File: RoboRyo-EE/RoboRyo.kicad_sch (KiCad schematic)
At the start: 78 parts, among them IC2 LD29080DT33R, IC3 LD29080DT50R, J1 2601-1103_000-004, J2 2601-1103_000-004, J3 2601-1103_000-004, J4 2601-1103_000-004, J5 2601-1103_000-004, J6 2601-1103_000-004, J7 2601-1103_000-004, J8 2601-1103_000-004, Q1 DMG9926USD-13, Q2 DMG9926USD-13, Q3 DMG9926USD-13, Q4 DMG9926USD-13, Q5 DMG9926USD-13, Q6 DMG9926USD-13, Q7 CSD13383F4, U1 STM32F446RETx, U2 ATmega328P-MM, Y1 ABM3-16.000MHZ-D2Y-T

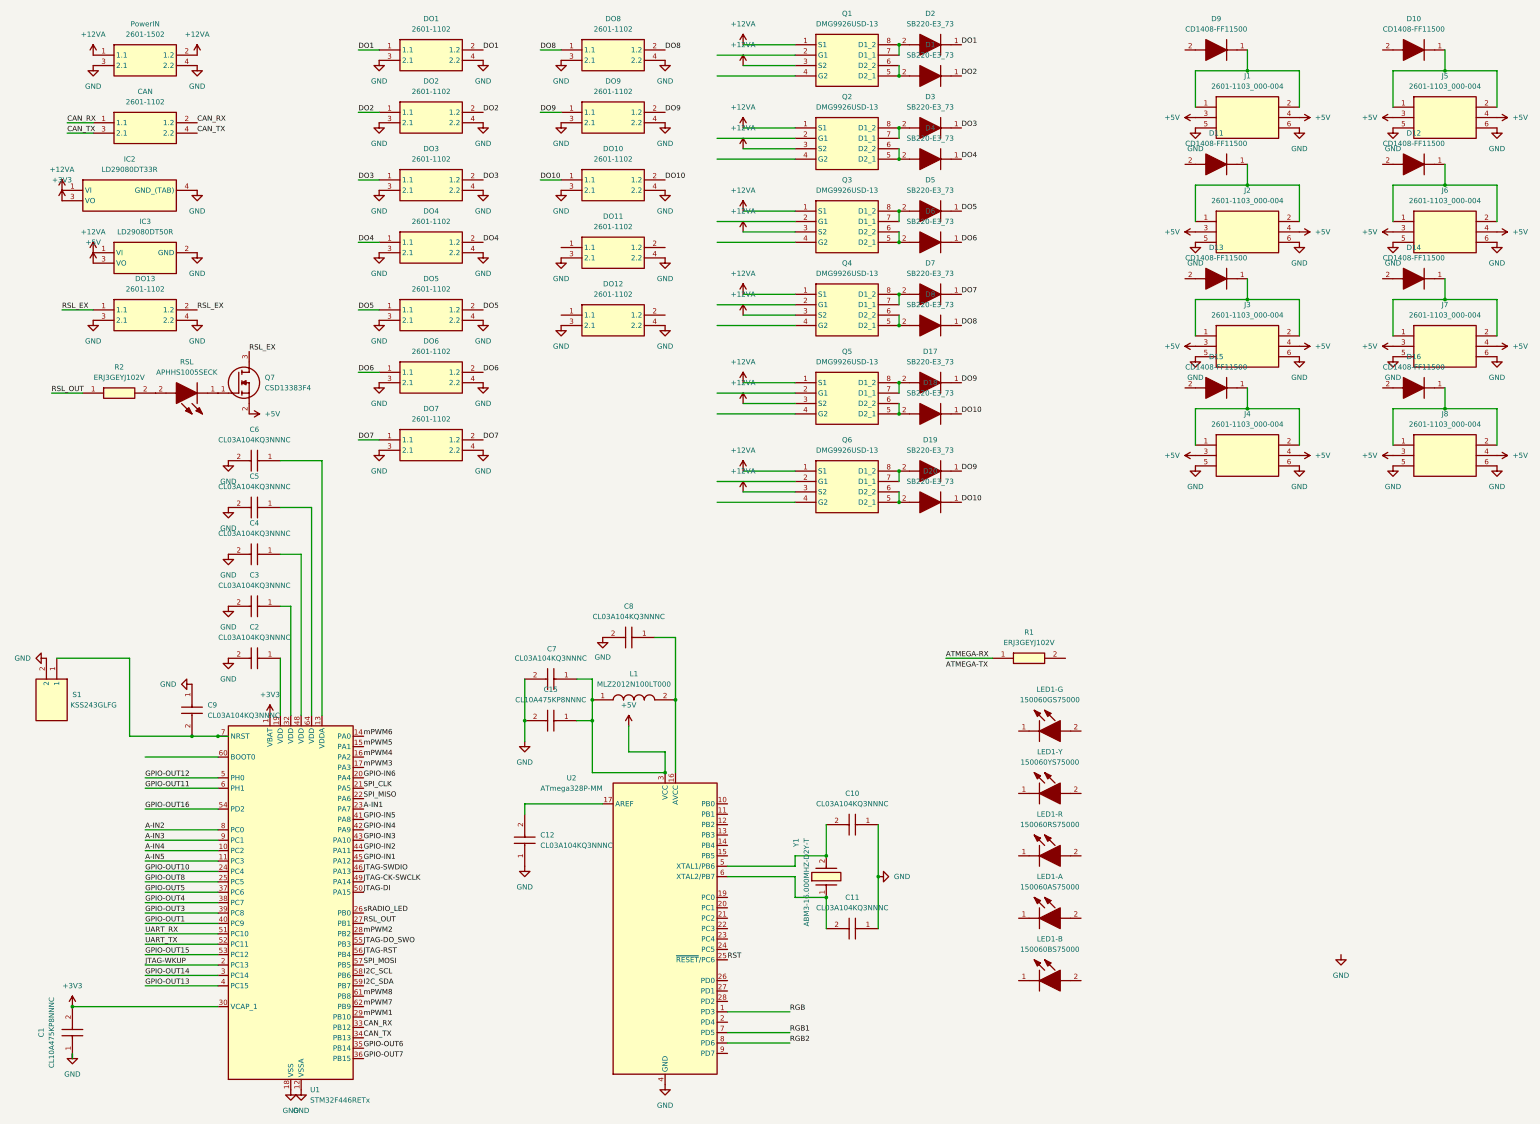
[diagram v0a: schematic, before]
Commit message: Sch New: IMU, Radio, PowerConfiguration
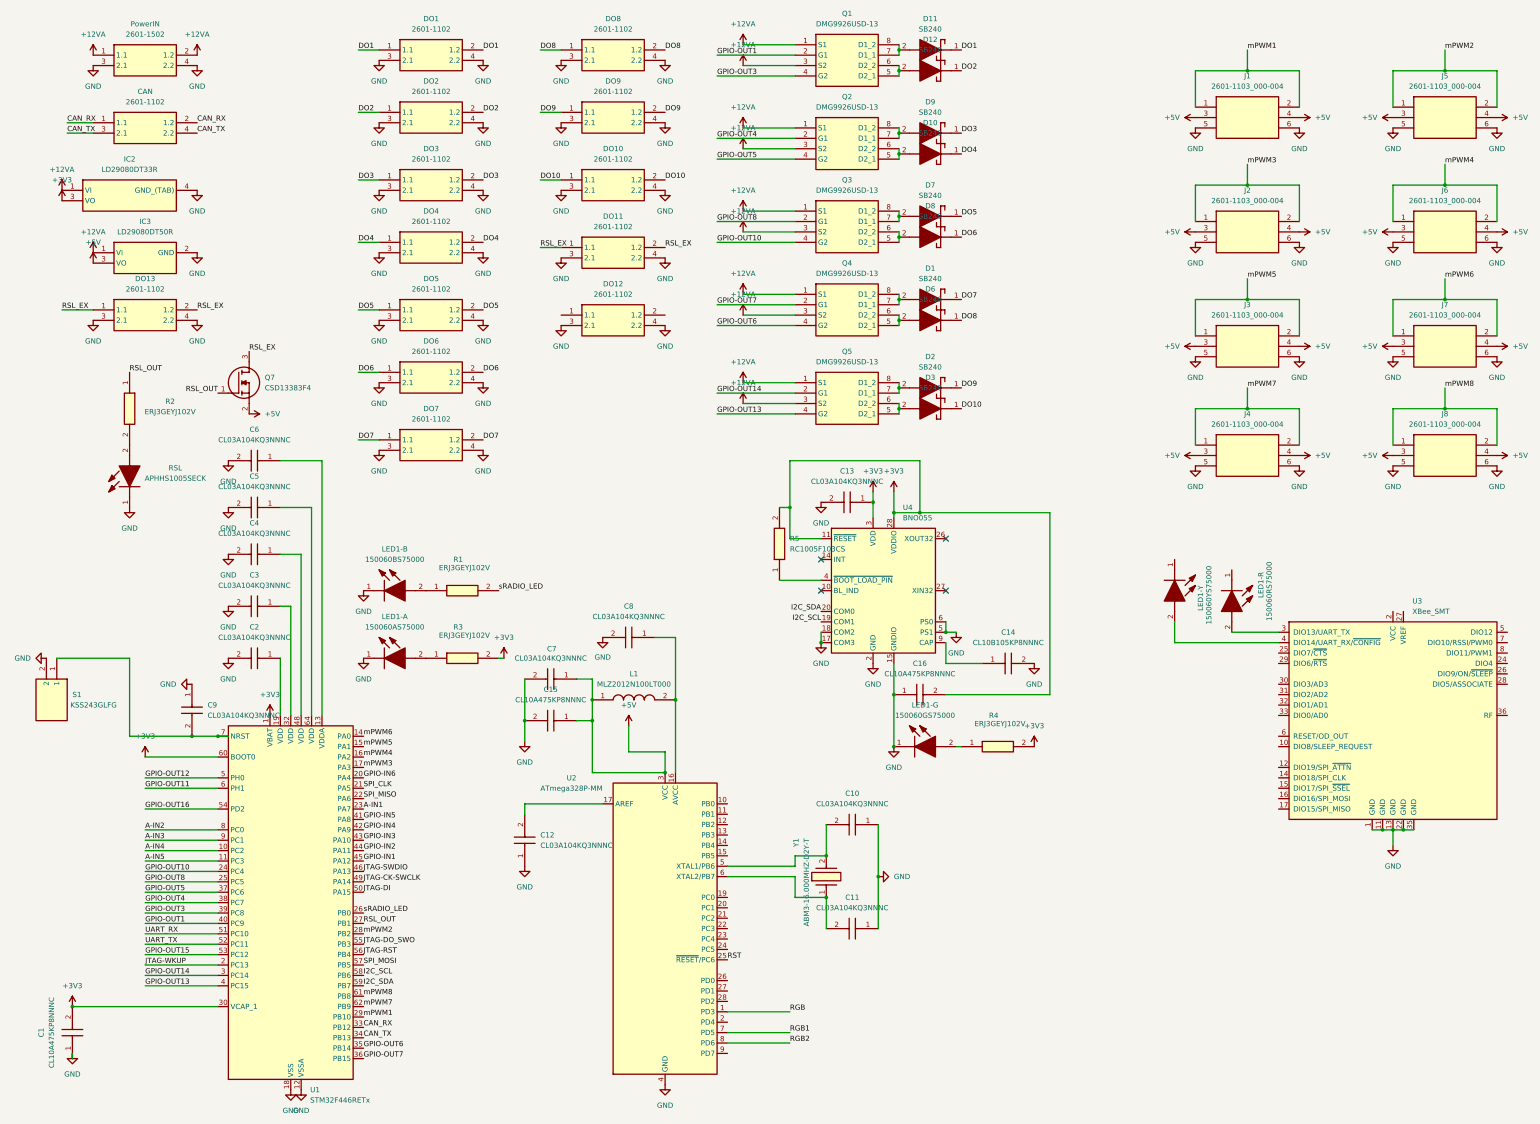
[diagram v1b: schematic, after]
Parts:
- removed D1, D17, D18, D19, D2, D20, D3, D4, D5, D6, D7, D8: SB220-E3_73, DIOAD1910W86L670D310, symbol SamacSys_Parts:SB220-E3_73
- removed D10, D11, D12, D13, D14, D15, D16, D9: CD1408-FF11500, DIOC3419X135N, symbol SamacSys_Parts:CD1408-FF11500
- removed Q6: DMG9926USD-13, SOIC127P600X175-8N, symbol SamacSys_Parts:DMG9926USD-13
- added C13: CL03A104KQ3NNNC, CAPC0603X33N, symbol SamacSys_Parts:CL03A104KQ3NNNC
- added C14: CL10B105KP8NNNC, CAPC1608X90N, symbol SamacSys_Parts:CL10B105KP8NNNC
- added C16: CL10A475KP8NNNC, CAPC1608X90N, symbol SamacSys_Parts:CL10A475KP8NNNC
- added D1, D10, D11, D12, D2, D3, D6, D7, D8, D9: SB240, DIOAD1910W86L670D310, symbol SamacSys_Parts:SB240
- added R3, R4: ERJ3GEYJ102V, ERJ3EKF1000V, symbol SamacSys_Parts:ERJ3GEYJ102V
- added R5: RC1005F103CS, RESC1005X40N, symbol SamacSys_Parts:RC1005F103CS
- added U3: XBee_SMT, RF_Module:Digi_XBee_SMT, symbol RF_ZigBee:XBee_SMT
- added U4: BNO055, Package_LGA:LGA-28_5.2x3.8mm_P0.5mm, symbol Sensor_Motion:BNO055
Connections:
- net ATMEGA-RX is gone; now on an unnamed net: R1.1
- net +3V3: now also U1.60 (BOOT0), C13.1, C16.2, R3.2, R4.2, R5.2, U4.11 (~{RESET}), U4.28 (VDDIO), U4.3 (VDD)
- net DO1: now also D11.1 (K)
- net DO10: now also D3.1 (K)
- net DO2: now also D12.1 (K)
- net DO3: now also D9.1 (K)
- net DO4: now also D10.1 (K)
- net DO5: now also D7.1 (K)
- net DO6: now also D8.1 (K)
- net DO7: now also D1.1 (K)
- net DO8: now also D6.1 (K)
- net DO9: now also D2.1 (K)
- net GND: now also LED1-A.1 (K), LED1-B.1 (K), LED1-G.1 (K), RSL.1 (K), C13.2, C14.2, C16.1, U3.1 (GND), U3.11 (GND), U3.13 (GND), U3.22 (GND), U3.35 (GND), U4.15 (GNDIO), U4.16 (GNDIO), U4.17 (COM3), U4.18 (COM2), U4.2 (GND), U4.25 (GNDIO), U4.5 (PS1), U4.6 (PS0)
- net GPIO-OUT1: now also Q1.2 (G1)
- net GPIO-OUT10: now also Q3.4 (G2)
- net GPIO-OUT13: now also Q5.4 (G2)
- net GPIO-OUT14: now also Q5.2 (G1)
- net GPIO-OUT3: now also Q1.4 (G2)
- net GPIO-OUT4: now also Q2.2 (G1)
- net GPIO-OUT5: now also Q2.4 (G2)
- net GPIO-OUT6: now also Q4.4 (G2)
- net GPIO-OUT7: now also Q4.2 (G1)
- net GPIO-OUT8: now also Q3.2 (G1)
- net I2C_SCL: now also U4.19 (COM1)
- net I2C_SDA: now also U4.20 (COM0)
- net RSL_EX: now also DO11.1 (1.1), DO11.2 (1.2)
- net RSL_OUT: now also Q7.1 (G)
- net mPWM1: now also J1.1 (1.1), J1.2 (1.2)
- net mPWM2: now also J5.1 (1.1), J5.2 (1.2)
- net mPWM3: now also J2.1 (1.1), J2.2 (1.2)
- net mPWM4: now also J6.1 (1.1), J6.2 (1.2)
- net mPWM5: now also J3.1 (1.1), J3.2 (1.2)
- net mPWM6: now also J7.1 (1.1), J7.2 (1.2)
- net mPWM7: now also J4.1 (1.1), J4.2 (1.2)
- net mPWM8: now also J8.1 (1.1), J8.2 (1.2)
- net sRADIO_LED: now also R1.2
- net at Q4.5 (D2_1), Q4.6 (D2_2): now also D6.2 (A)
- net at Q4.7 (D1_1), Q4.8 (D1_2): now also D1.2 (A)
- net at LED1-A.2 (A): now also R3.1
- net at Q1.7 (D1_1), Q1.8 (D1_2): now also D11.2 (A)
- net at Q1.5 (D2_1), Q1.6 (D2_2): now also D12.2 (A)
- net at Q3.5 (D2_1), Q3.6 (D2_2): now also D8.2 (A)
- net at Q2.7 (D1_1), Q2.8 (D1_2): now also D9.2 (A)
- net at LED1-R.2 (A): now also U3.3 (DIO13/UART_TX)
- net at Q3.7 (D1_1), Q3.8 (D1_2): now also D7.2 (A)
- net at LED1-Y.2 (A): now also U3.4 (DIO14/UART_RX/~{CONFIG})
- net at Q5.7 (D1_1), Q5.8 (D1_2): now also D2.2 (A)
- net at Q5.5 (D2_1), Q5.6 (D2_2): now also D3.2 (A)
- net at Q2.5 (D2_1), Q2.6 (D2_2): now also D10.2 (A)
- net at LED1-G.2 (A): now also R4.1
- new net: R5.1, U4.4 (~{BOOT_LOAD_PIN})
- new net: C14.1, U4.9 (CAP)
- no-connect marks 0 -> 4
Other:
- moved on the sheet: LED1-A, LED1-B, LED1-G, LED1-R, LED1-Y, R2, RSL

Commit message: Sch Complete, PCB: General Layout complete, wiring left
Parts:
- removed C10, C11, C12, C7, C8: CL03A104KQ3NNNC, CAPC0603X33N, symbol SamacSys_Parts:CL03A104KQ3NNNC
- removed C15: CL10A475KP8NNNC, CAPC1608X90N, symbol SamacSys_Parts:CL10A475KP8NNNC
- removed L1: MLZ2012N100LT000, INDC2012X105N, symbol SamacSys_Parts:MLZ2012N100LT000
- removed LED1-R: 150060RS75000, LEDC1608X80N, symbol SamacSys_Parts:150060RS75000
- removed LED1-Y: 150060YS75000, LEDC1608X80N, symbol SamacSys_Parts:150060YS75000
- removed U2: ATmega328P-MM, Package_DFN_QFN:QFN-28-1EP_4x4mm_P0.45mm_EP2.4x2.4mm, symbol MCU_Microchip_ATmega:ATmega328P-MM
- removed U3: XBee_SMT, RF_Module:Digi_XBee_SMT, symbol RF_ZigBee:XBee_SMT
- removed Y1: ABM3-16.000MHZ-D2Y-T, ABM3, symbol SamacSys_Parts:ABM3-16.000MHZ-D2Y-T
- added IC1: XB24CAWIT-001, XB24CAWIT001, symbol SamacSys_Parts:XB24CAWIT-001
- added LED1-R1: 150060RS75000, LEDC1608X80N, symbol SamacSys_Parts:150060RS75000
- added LED1-Y1: 150060YS75000, LEDC1608X80N, symbol SamacSys_Parts:150060YS75000
- added R6, R7: ERJ-2RKF1001X, ERJ2RKD1004X, symbol SamacSys_Parts:ERJ-2RKF1001X
- renumbered CAN to CAN1, LED1-A to LED1-A1, LED1-B to LED1-B1, LED1-G to LED1-G1, PowerIN to PowerIN1, RSL to RSL1
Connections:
- net +3V3: now also IC1.1 (VCC)
- net GND: now also IC1.10 (GND), LED1-R1.1 (K), LED1-Y1.1 (K)
- net UART_RX renamed Radio_UART_RX
- net Radio_UART_RX: now also IC1.3 (DIN/~{CONFIG})
- net UART_TX renamed Radio_UART_TX
- net Radio_UART_TX: now also IC1.2 (DOUT)
- new net: LED1-Y1.2 (A), R7.2
- new net: IC1.13 (ON/~{SLEEP}), R7.1
- new net: IC1.15 (DIO5/ASSOC), R6.1
- new net: LED1-R1.2 (A), R6.2
- no-connect marks 4 -> 17
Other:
- moved on the sheet: C13, C14, C16, LED1-A1, LED1-B1, LED1-G1, Q7, R1, R2, R3, R4, R5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

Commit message: Sch Edited: I am stupid, PCB:Pending Completition
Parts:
- added D4: NRVHP260SFT3G, SODFL3616X98N, symbol SamacSys_Parts:NRVHP260SFT3G
- added D5: CD1408-FF11500, DIOC3419X135N, symbol SamacSys_Parts:CD1408-FF11500
- added JTAG1: ~, symbol Connectors:JTAG
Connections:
- net +12VA: no longer Q1.1 (S1), Q1.3 (S2), Q2.1 (S1), Q2.3 (S2), Q3.1 (S1), Q3.3 (S2), Q4.1 (S1), Q4.3 (S2), Q5.1 (S1), Q5.3 (S2)
- net +3V3: now also C2.1, C3.1, C4.1, C5.1, C6.1, U1.13 (VDDA), U1.19 (VDD), U1.32 (VDD), U1.48 (VDD), U1.64 (VDD), D4.1 (K); no longer IC2.3 (VO)
- net +5V: now also DO11.1 (1.1), DO11.2 (1.2), D5.1 (K); no longer IC3.3 (VO), Q7.2 (S)
- net GND: now also Q1.1 (S1), Q1.3 (S2), Q2.1 (S1), Q2.3 (S2), Q3.1 (S1), Q3.3 (S2), Q4.1 (S1), Q4.3 (S2), Q5.1 (S1), Q5.3 (S2), Q7.2 (S), JTAG1. (GND); no longer DO11.3 (2.1), DO11.4 (2.2)
- net JTAG-CK-SWCLK: now also JTAG1.2 (JTAG-CK-SWCLK)
- net JTAG-DI: now also JTAG1.5 (JTAG-DI)
- net JTAG-DO_SWO: now also JTAG1.4 (JTAG-DO_SWO)
- net JTAG-RST: now also JTAG1.3 (JTAG-RST)
- net JTAG-SWDIO: now also JTAG1.1 (JTAG-SWDIO)
- net JTAG-WKUP: now also JTAG1.0 (JTAGWKUP)
- net RSL_EX: now also DO11.3 (2.1), DO11.4 (2.2); no longer DO11.1 (1.1), DO11.2 (1.2)
- new net: D5.2 (A), IC3.3 (VO)
- new net: D4.2 (A), IC2.3 (VO)
